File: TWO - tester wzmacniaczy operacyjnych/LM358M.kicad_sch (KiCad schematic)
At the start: 20 parts, among them J1 Conn_01x01, U2 LM358

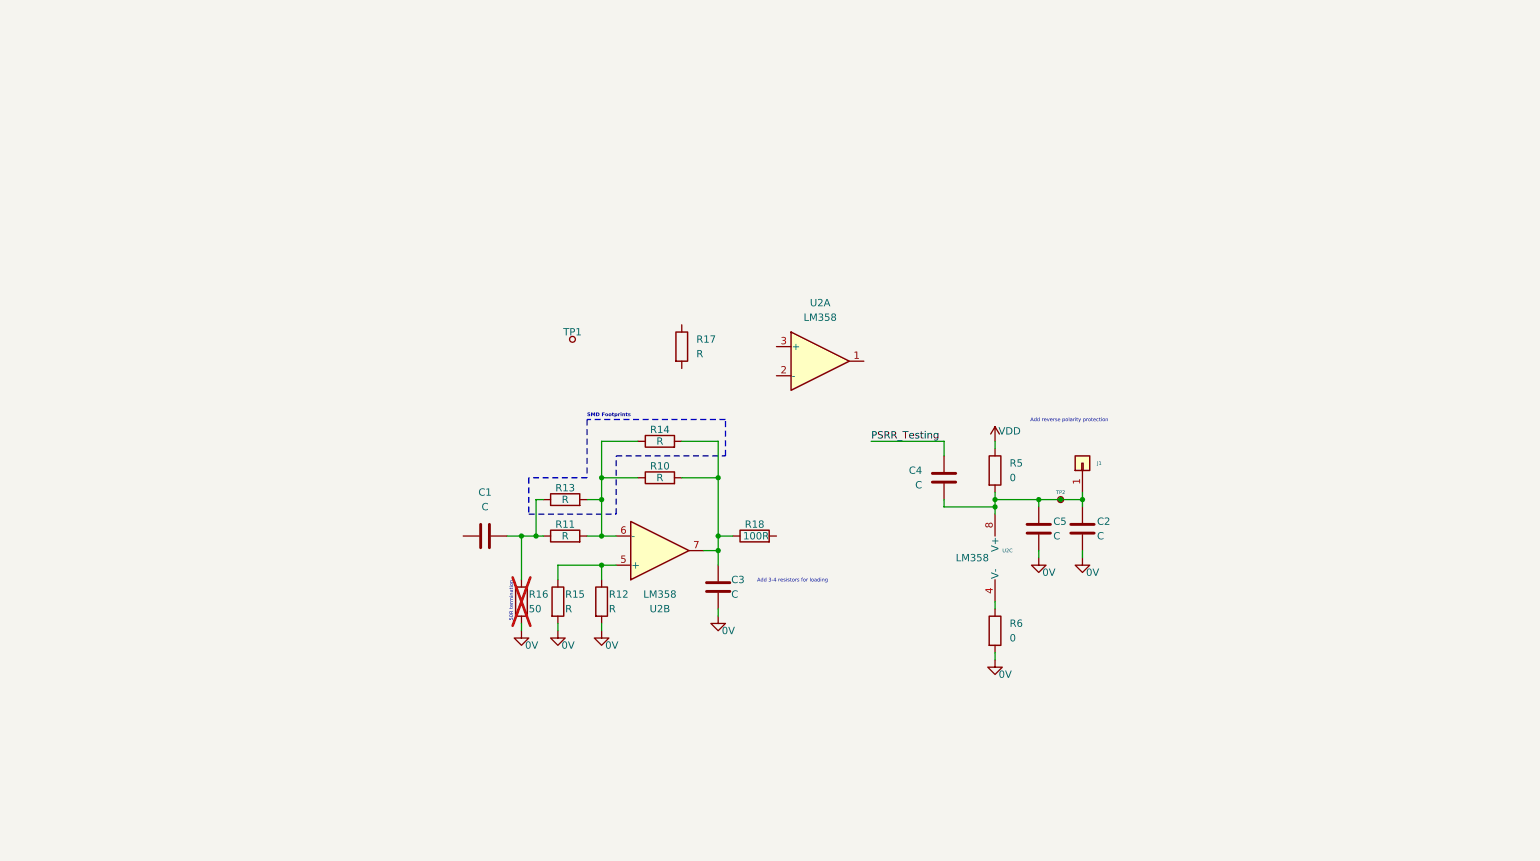
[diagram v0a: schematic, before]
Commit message: Split OPA358 into part A and B Clean reference designator, test points, connectors
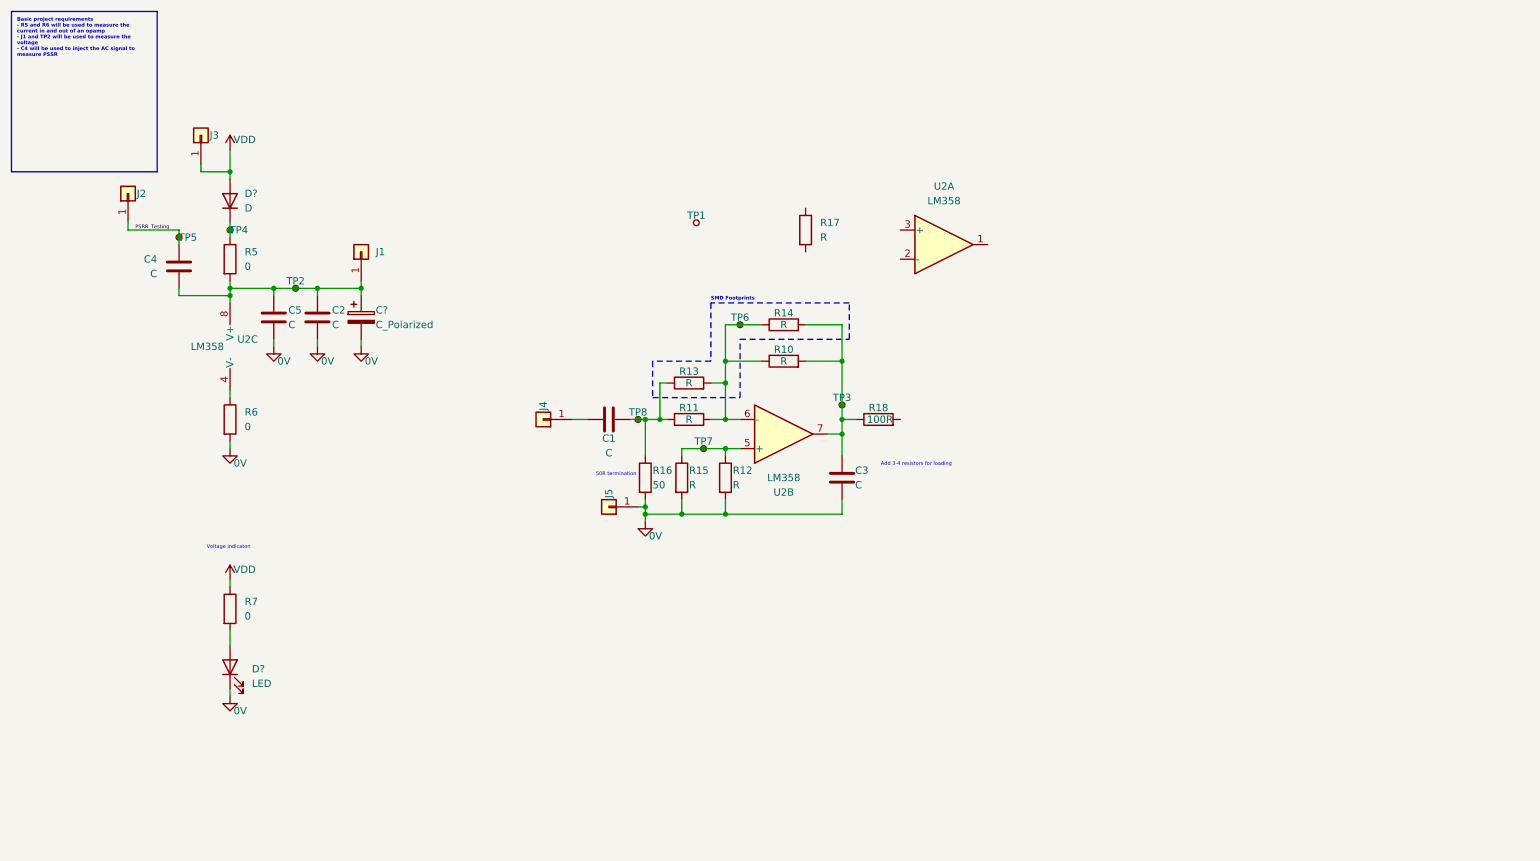
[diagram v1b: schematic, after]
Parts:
- added C?: C_Polarized, symbol Device:C_Polarized
- added D?: LED, symbol Device:LED
- added D?: D, symbol Device:D
- added J2, J3, J4, J5: Conn_01x01, Connector_PinHeader_2.54mm:PinHeader_1x01_P2.54mm_Vertical, symbol Connector_Generic:Conn_01x01
- added R7: 0, symbol Device:R
- added TP3, TP4, TP5, TP6, TP7, TP8: TestPoint_Small, symbol Connector:TestPoint_Small
- C1: footprint (none) -> Capacitor_THT:C_Disc_D3.8mm_W2.6mm_P2.50mm
- R16: now fitted
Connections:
- net 0V: now also C?.2, D?.1 (K), J5.1 (Pin_1)
- net PSRR_Testing: now also J2.1 (Pin_1), TP5.1
- net VDD: now also D?.2 (A), J3.1 (Pin_1), R7.1; no longer R5.1
- net at C2.1, C4.2, C5.1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: now also C?.1
- net at R10.1, R11.2, R13.2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: now also TP6.1
- net at C3.2, R10.2, R14.2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: now also TP3.1
- net at C1.2, R11.1, R13.1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: now also TP8.1
- net at R12.1, R15.1, U2.5 (+): now also TP7.1
- net at C1.1: now also J4.1 (Pin_1)
- new net: D?.2 (A), R7.2
- new net: D?.1 (K), R5.1, TP4.1
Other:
- note added: "Voltage indicaton"
- note removed: "Add reverse polarity protection"
- moved on the sheet: C1, C2, C3, C4, C5, J1, R10, R11, R12, R13, R14, R15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

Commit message: Add change according to LM358 component once again
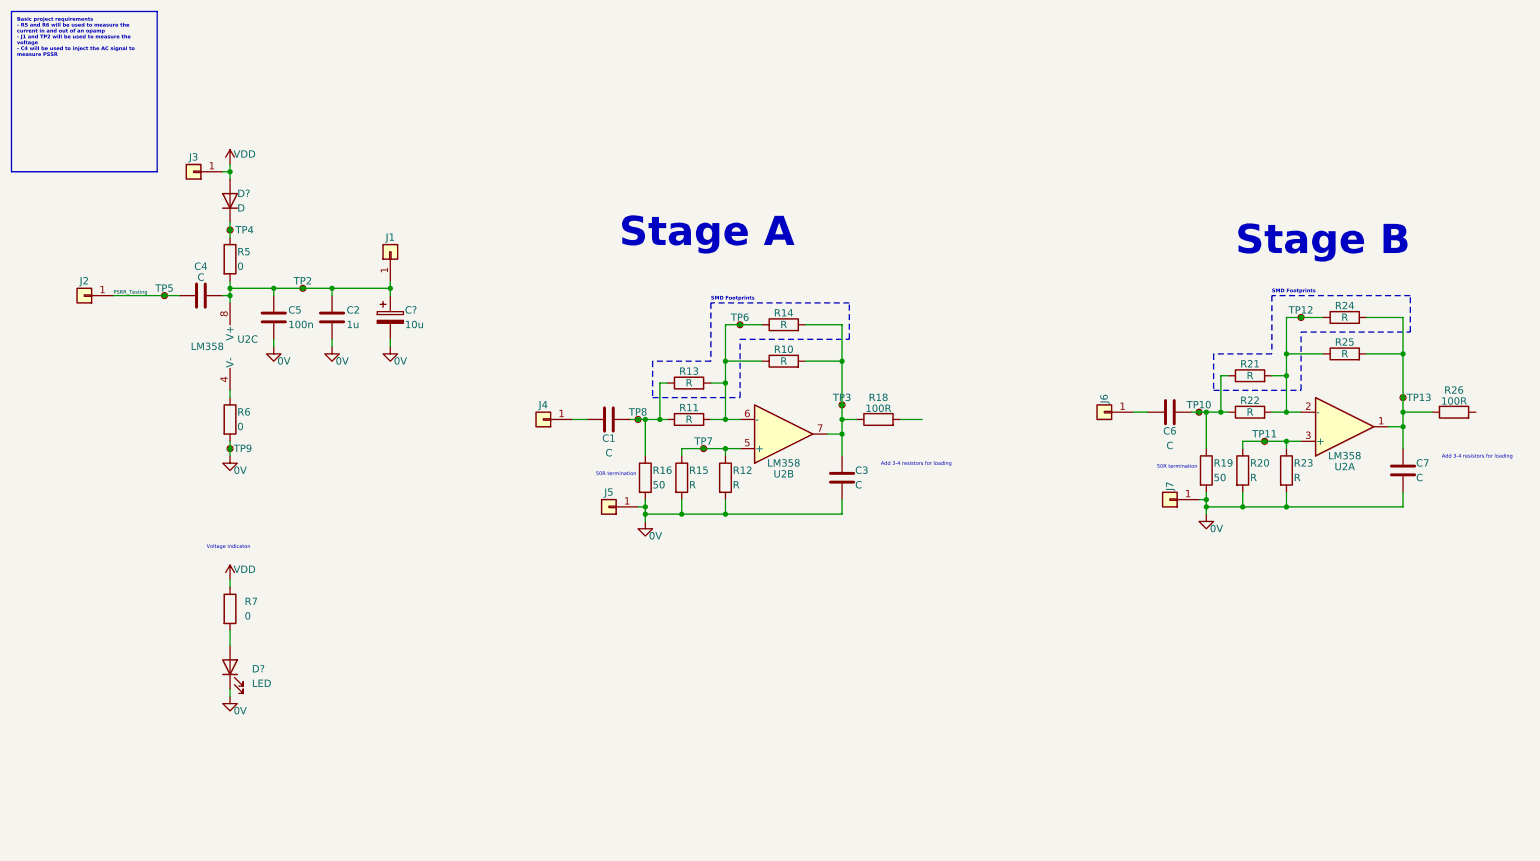
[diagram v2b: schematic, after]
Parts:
- removed R17: R, symbol Device:R
- removed TP1: TestPoint_Small, symbol Connector:TestPoint_Small
- added C6: C, Capacitor_THT:C_Disc_D3.8mm_W2.6mm_P2.50mm, symbol Device:C
- added C7: C, symbol Device:C
- added J6, J7: Conn_01x01, Connector_PinHeader_2.54mm:PinHeader_1x01_P2.54mm_Vertical, symbol Connector_Generic:Conn_01x01
- added R19: 50, symbol Device:R
- added R20, R21, R24: R, Resistor_SMD:R_0805_2012Metric, symbol Device:R
- added R22, R23, R25: R, Resistor_THT:R_Axial_DIN0207_L6.3mm_D2.5mm_P10.16mm_Horizontal, symbol Device:R
- added R26: 100R, symbol Device:R
- added TP10, TP11, TP12, TP13, TP9: TestPoint_Small, symbol Connector:TestPoint_Small
- C2: value C -> 1u
- C5: value C -> 100n
- C?: value C_Polarized -> 10u
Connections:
- net 0V: now also C7.1, J7.1 (Pin_1), R19.2, R20.2, R23.2, TP9.1
- net at U2.1: now also C7.2, R24.2, R25.2, R26.1, TP13.1
- net at U2.2 (-): now also R21.2, R22.2, R24.1, R25.1, TP12.1
- net at U2.3 (+): now also R20.1, R23.1, TP11.1
- new net: C6.2, R19.1, R21.1, R22.1, TP10.1
- new net: C6.1, J6.1 (Pin_1)
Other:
- note added: "Stage A"
- note added: "Stage B"
- moved on the sheet: C2, C4, C?, J1, J2, J3, TP2, TP5, U2A

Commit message: Modify LM358N sheet and m324N
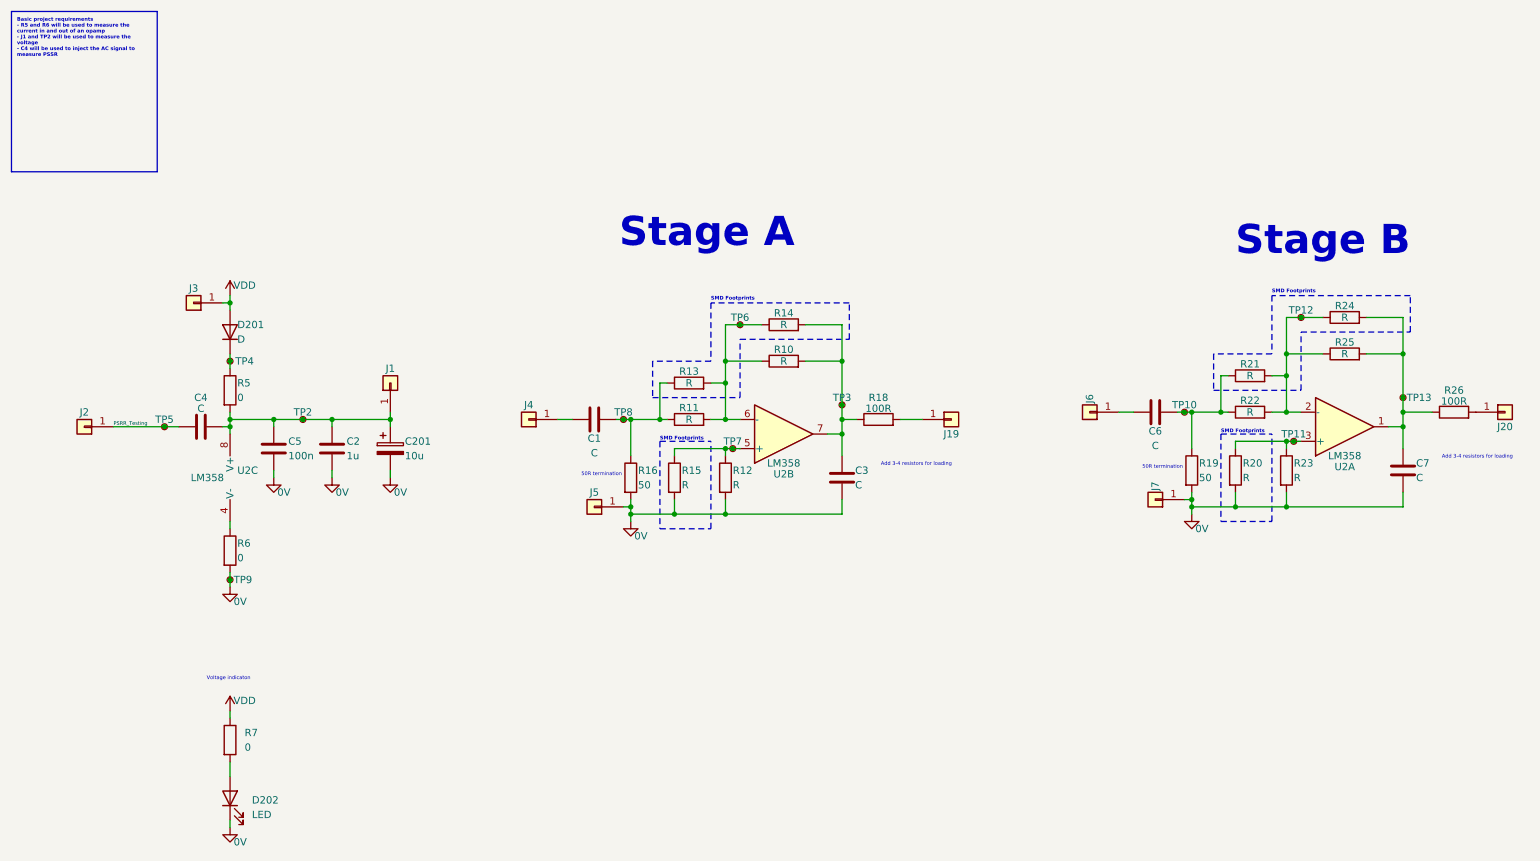
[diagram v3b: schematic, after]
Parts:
- added J19, J20: Conn_01x01, Connector_PinHeader_2.54mm:PinHeader_1x01_P2.54mm_Vertical, symbol Connector_Generic:Conn_01x01
- gave numbers to parts that had none: 3
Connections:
- net at R26.2: now also J20.1 (Pin_1)
- net at R18.2: now also J19.1 (Pin_1)
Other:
- moved on the sheet: C1, C2, C201, C4, C5, C6, D201, D202, J1, J2, J3, J4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
